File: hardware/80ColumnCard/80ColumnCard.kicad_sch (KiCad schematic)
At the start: 36 parts, among them J1 Apple II Expansion Bus, J2 VIDEO & LIGHT PEN, Q1 2N3904, U1 74LS86, U14 74LS157, U15 74LS157, U16 74LS157, U18 74LS273, U19 MC6845, U2 74LS02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

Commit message: DEV->DEVICE_SELECT
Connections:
- net DEV renamed DEVICE_SELECT
- net ~{DEV} renamed ~{DEVICE_SELECT}
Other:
- moved on the sheet: J1

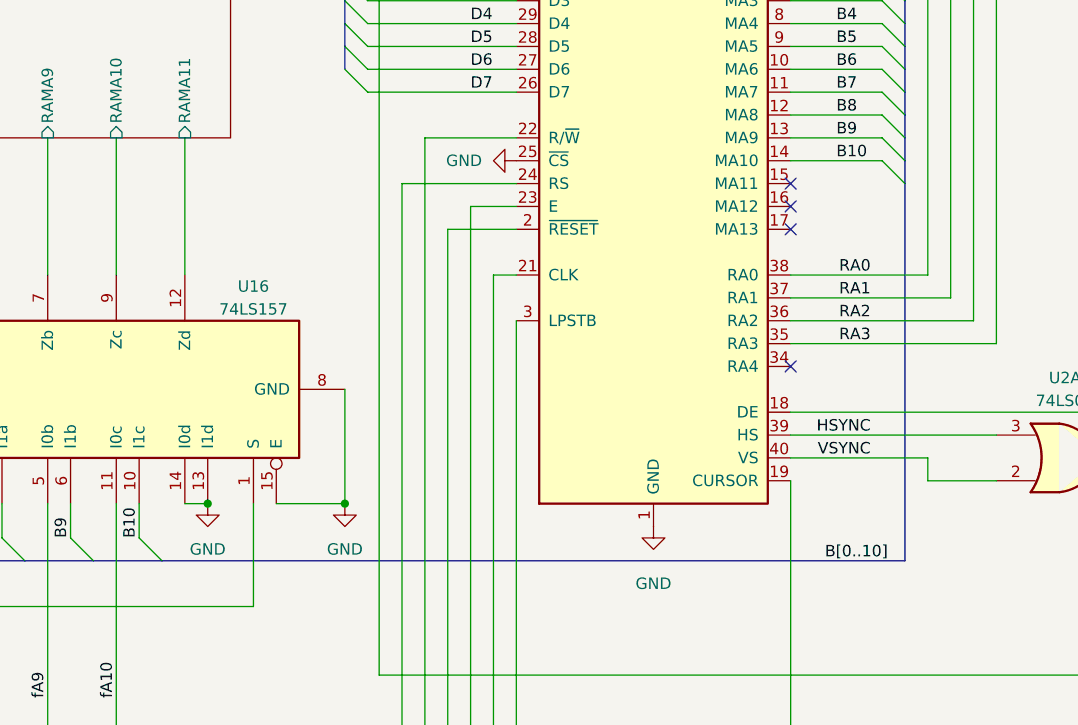
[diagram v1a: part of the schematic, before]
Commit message: connect CRTC A11 to SRAM multiplexer. add jumpers for selectable firmware
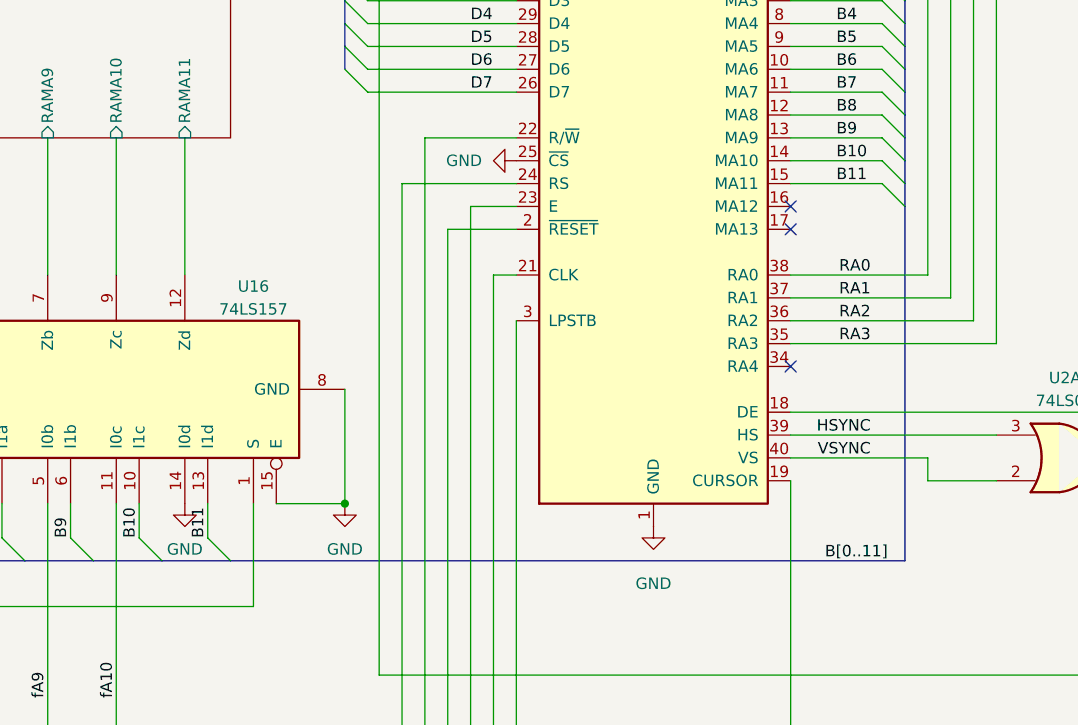
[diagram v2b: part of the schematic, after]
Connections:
- net GND: no longer U16.13 (I1d)
- net B11: now reaches U19.15 (MA11)
- net B11: now also U16.13 (I1d)
- no-connect marks 22 -> 21
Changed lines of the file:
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@@
   (junction (at 60.96 165.1) (diameter 0) (color 0 0 0 0)
   )
-  (junction (at 298.45 167.64) (diameter 0) (color 0 0 0 0)
-  )
   (junction (at 116.84 264.16) (diameter 0) (color 0 0 0 0)
   )
@@
   (no_connect (at 412.75 227.33))
   (no_connect (at 452.12 191.77))
-  (no_connect (at 363.22 132.08))
   (no_connect (at 170.18 40.64))
   (no_connect (at 452.12 186.69))
@@
     (stroke (width 0) (type default) (color 0 0 0 0))
   )
+  (bus_entry (at 298.45 171.45) (size 2.54 2.54)
+    (stroke (width 0) (type default) (color 0 0 0 0))
+  )
   (bus_entry (at 316.23 121.92) (size -2.54 -2.54)
     (stroke (width 0) (type default) (color 0 0 0 0))
@@
     (stroke (width 0) (type default) (color 0 0 0 0))
   )
+  (bus_entry (at 373.38 132.08) (size 2.54 2.54)
+    (stroke (width 0) (type default) (color 0 0 0 0))
+  )
   (bus_entry (at 373.38 129.54) (size 2.54 2.54)
     (stroke (width 0) (type default) (color 0 0 0 0))
@@
     (stroke (width 0) (type default) (color 0 0 0 0))
   )
+  (wire (pts (xy 298.45 167.64) (xy 298.45 171.45))
+    (stroke (width 0) (type default) (color 0 0 0 0))
+  )
   (wire (pts (xy 100.33 261.62) (xy 137.16 261.62))
     (stroke (width 0) (type default) (color 0 0 0 0))
@@
     (stroke (width 0) (type default) (color 0 0 0 0))
   )
+  (bus (pts (xy 300.99 173.99) (xy 375.92 173.99))
+    (stroke (width 0) (type default) (color 0 0 0 0))
+  )
   (wire (pts (xy 275.59 167.64) (xy 275.59 171.45))
     (stroke (width 0) (type default) (color 0 0 0 0))
@@
     (stroke (width 0) (type default) (color 0 0 0 0))
   )
+  (bus (pts (xy 375.92 134.62) (xy 375.92 173.99))
+    (stroke (width 0) (type default) (color 0 0 0 0))
+  )
   (wire (pts (xy 127 58.42) (xy 196.85 58.42))
     (stroke (width 0) (type default) (color 0 0 0 0))
@@
     (stroke (width 0) (type default) (color 0 0 0 0))
   )
-  (bus (pts (xy 293.37 173.99) (xy 375.92 173.99))
+  (bus (pts (xy 293.37 173.99) (xy 300.99 173.99))
     (stroke (width 0) (type default) (color 0 0 0 0))
   )
@@
     (stroke (width 0) (type default) (color 0 0 0 0))
   )
-  (bus (pts (xy 375.92 132.08) (xy 375.92 173.99))
+  (bus (pts (xy 375.92 132.08) (xy 375.92 134.62))
     (stroke (width 0) (type default) (color 0 0 0 0))
   )
@@
     (stroke (width 0) (type default) (color 0 0 0 0))
   )
-  (wire (pts (xy 295.91 167.64) (xy 298.45 167.64))
-    (stroke (width 0) (type default) (color 0 0 0 0))
-  )
   (wire (pts (xy 95.25 204.47) (xy 67.31 204.47))
     (stroke (width 0) (type default) (color 0 0 0 0))
@@
     (stroke (width 0) (type default) (color 0 0 0 0))
   )
+  (wire (pts (xy 363.22 132.08) (xy 373.38 132.08))
+    (stroke (width 0) (type default) (color 0 0 0 0))
+  )
   (wire (pts (xy 224.79 167.64) (xy 224.79 171.45))
     (stroke (width 0) (type default) (color 0 0 0 0))
@@
     (effects (font (size 1.27 1.27)) (justify left bottom))
   )
+  (label "B11" (at 298.45 171.45 90)
+    (effects (font (size 1.27 1.27)) (justify left bottom))
+  )
   (label "A14" (at 535.94 60.96 0)
     (effects (font (size 1.27 1.27)) (justify left bottom))
@@
     (effects (font (size 1.27 1.27)) (justify left bottom))
   )
-  (label "B[0..10]" (at 367.03 173.99 0)
+  (label "B[0..11]" (at 367.03 173.99 0)
     (effects (font (size 1.27 1.27)) (justify left bottom))
   )
@@
     (effects (font (size 1.27 1.27)) (justify left bottom))
   )
+  (label "B11" (at 368.3 132.08 0)
+    (effects (font (size 1.27 1.27)) (justify left bottom))
+  )
   (label "DMA_IN" (at 579.12 81.28 180)
     (effects (font (size 1.27 1.27)) (justify right bottom))
@@
     (pin "1")
   )
-  (symbol (lib_id "power:GND") (at 298.45 167.64 0) (unit 1)
+  (symbol (lib_id "power:GND") (at 295.91 167.64 0) (unit 1)
     (in_bom yes) (on_board yes) (fields_autoplaced)
-    (property "Reference" "#PWR0140" (id 0) (at 298.45 173.99 0)
+    (property "Reference" "#PWR0140" (id 0) (at 295.91 173.99 0)
       (effects (font (size 1.27 1.27)) hide)
     )
-    (property "Value" "GND" (id 1) (at 298.45 172.72 0))
-    (property "Footprint" "" (id 2) (at 298.45 167.64 0)
+    (property "Value" "GND" (id 1) (at 295.91 172.72 0))
+    (property "Footprint" "" (id 2) (at 295.91 167.64 0)
       (effects (font (size 1.27 1.27)) hide)
     )
-    (property "Datasheet" "" (id 3) (at 298.45 167.64 0)
+    (property "Datasheet" "" (id 3) (at 295.91 167.64 0)
       (effects (font (size 1.27 1.27)) hide)
     )
@@
       (reference "#PWR0108") (unit 1) (value "GND") (footprint "")
     )
+    (path "/3653aa16-49ad-4f73-9584-b2d8a31551f4/02f37925-db2f-4b32-9416-ee76e88990e0"
+      (reference "#PWR0109") (unit 1) (value "+5V") (footprint "")
+    )
     (path "/3653aa16-49ad-4f73-9584-b2d8a31551f4/f3066ec5-9040-45a1-98d8-a8bfe2d10528"
       (reference "#PWR0110") (unit 1) (value "GND") (footprint "")
@@
       (reference "J2") (unit 1) (value "VIDEO & LIGHT PEN") (footprint "Connector_PinHeader_2.54mm:PinHeader_1x06_P2.54mm_Horizontal")
     )
+    (path "/3653aa16-49ad-4f73-9584-b2d8a31551f4/9f10952b-85b8-4d29-82d9-c4db269f5aa8"
+      (reference "JP1") (unit 1) (value "A10") (footprint "Connector_PinHeader_2.54mm:PinHeader_1x03_P2.54mm_Vertical")
+    )
+    (path "/3653aa16-49ad-4f73-9584-b2d8a31551f4/ceecdba2-9510-4d35-8da5-2f03008ae102"
+      (reference "JP2") (unit 1) (value "A11") (footprint "Connector_PinHeader_2.54mm:PinHeader_1x03_P2.54mm_Vertical")
+    )
     (path "/5c0e70ea-1119-414b-9aa5-6f54e9ab44e4"

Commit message: clean up, add jumpers for fw/char selection
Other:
- moved on the sheet: C3, C5, J2, Q1, R1, R10, R11, R12, R13, R2, R9, U1A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

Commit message: add some annotations
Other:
- note added: "Char width select"
- note added: "Combined sync"
- note added: "Display enable"
- note added: "Invert signal"
- note added: "Pixel data"
- note added: "SRAM page select"
- note added: "Start at 4 or 5 and count up to 12 to draw either 8 or 9 pixels"
- note added: "video signal"
- moved on the sheet: U4F, U6D
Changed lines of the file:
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@@
   (junction (at 220.98 251.46) (diameter 0) (color 0 0 0 0)
   )
-  (junction (at 160.02 179.07) (diameter 0) (color 0 0 0 0)
-  )
   (junction (at 128.27 189.23) (diameter 0) (color 0 0 0 0)
   )
@@
   (junction (at 41.91 76.2) (diameter 0) (color 0 0 0 0)
   )
+  (junction (at 168.91 179.07) (diameter 0) (color 0 0 0 0)
+  )
   (junction (at 209.55 71.12) (diameter 0) (color 0 0 0 0)
   )
@@
     (stroke (width 0) (type default) (color 0 0 0 0))
   )
-  (wire (pts (xy 128.27 189.23) (xy 154.94 189.23))
+  (wire (pts (xy 128.27 189.23) (xy 149.86 189.23))
     (stroke (width 0) (type default) (color 0 0 0 0))
   )
@@
     (stroke (width 0) (type default) (color 0 0 0 0))
   )
+  (wire (pts (xy 168.91 179.07) (xy 201.93 179.07))
+    (stroke (width 0) (type default) (color 0 0 0 0))
+  )
   (wire (pts (xy 415.29 181.61) (xy 415.29 157.48))
     (stroke (width 0) (type default) (color 0 0 0 0))
@@
     (stroke (width 0) (type default) (color 0 0 0 0))
   )
-  (wire (pts (xy 474.98 196.85) (xy 474.98 219.71))
+  (wire (pts (xy 464.82 196.85) (xy 464.82 219.71))
     (stroke (width 0) (type default) (color 0 0 0 0))
   )
@@
     (stroke (width 0) (type default) (color 0 0 0 0))
   )
-  (wire (pts (xy 100.33 153.67) (xy 138.43 153.67))
+  (wire (pts (xy 100.33 153.67) (xy 133.35 153.67))
     (stroke (width 0) (type default) (color 0 0 0 0))
   )
@@
     (stroke (width 0) (type default) (color 0 0 0 0))
   )
-  (wire (pts (xy 154.94 189.23) (xy 154.94 163.83))
+  (wire (pts (xy 149.86 172.72) (xy 149.86 189.23))
     (stroke (width 0) (type default) (color 0 0 0 0))
   )
@@
     (stroke (width 0) (type default) (color 0 0 0 0))
   )
-  (wire (pts (xy 426.72 219.71) (xy 474.98 219.71))
+  (wire (pts (xy 426.72 219.71) (xy 464.82 219.71))
     (stroke (width 0) (type default) (color 0 0 0 0))
   )
@@
     (stroke (width 0) (type default) (color 0 0 0 0))
   )
-  (wire (pts (xy 97.79 237.49) (xy 97.79 207.01))
+  (wire (pts (xy 97.79 237.49) (xy 97.79 217.17))
     (stroke (width 0) (type default) (color 0 0 0 0))
   )
@@
     (stroke (width 0) (type default) (color 0 0 0 0))
   )
-  (wire (pts (xy 153.67 153.67) (xy 162.56 153.67))
+  (wire (pts (xy 148.59 153.67) (xy 149.86 153.67))
     (stroke (width 0) (type default) (color 0 0 0 0))
   )
@@
     (stroke (width 0) (type default) (color 0 0 0 0))
   )
+  (wire (pts (xy 168.91 170.18) (xy 167.64 170.18))
+    (stroke (width 0) (type default) (color 0 0 0 0))
+  )
   (wire (pts (xy 158.75 255.27) (xy 173.99 255.27))
     (stroke (width 0) (type default) (color 0 0 0 0))
@@
     (stroke (width 0) (type default) (color 0 0 0 0))
   )
+  (wire (pts (xy 130.81 179.07) (xy 168.91 179.07))
+    (stroke (width 0) (type default) (color 0 0 0 0))
+  )
   (wire (pts (xy 196.85 58.42) (xy 196.85 88.9))
     (stroke (width 0) (type default) (color 0 0 0 0))
@@
     (stroke (width 0) (type default) (color 0 0 0 0))
   )
-  (wire (pts (xy 154.94 163.83) (xy 157.48 163.83))
-    (stroke (width 0) (type default) (color 0 0 0 0))
-  )
   (wire (pts (xy 212.09 73.66) (xy 325.12 73.66))
     (stroke (width 0) (type default) (color 0 0 0 0))
@@
     (stroke (width 0) (type default) (color 0 0 0 0))
   )
-  (wire (pts (xy 276.86 207.01) (xy 276.86 241.3))
+  (wire (pts (xy 276.86 217.17) (xy 276.86 241.3))
     (stroke (width 0) (type default) (color 0 0 0 0))
   )
@@
     (stroke (width 0) (type default) (color 0 0 0 0))
   )
+  (wire (pts (xy 149.86 172.72) (xy 152.4 172.72))
+    (stroke (width 0) (type default) (color 0 0 0 0))
+  )
   (wire (pts (xy 434.34 170.18) (xy 434.34 186.69))
     (stroke (width 0) (type default) (color 0 0 0 0))
@@
     (stroke (width 0) (type default) (color 0 0 0 0))
   )
+  (wire (pts (xy 149.86 167.64) (xy 152.4 167.64))
+    (stroke (width 0) (type default) (color 0 0 0 0))
+  )
   (wire (pts (xy 177.8 201.93) (xy 327.66 201.93))
     (stroke (width 0) (type default) (color 0 0 0 0))
@@
     (stroke (width 0) (type default) (color 0 0 0 0))
   )
+  (wire (pts (xy 168.91 170.18) (xy 168.91 179.07))
+    (stroke (width 0) (type default) (color 0 0 0 0))
+  )
   (wire (pts (xy 535.94 33.02) (xy 551.18 33.02))
     (stroke (width 0) (type default) (color 0 0 0 0))
@@
     (stroke (width 0) (type default) (color 0 0 0 0))
   )
-  (wire (pts (xy 97.79 207.01) (xy 276.86 207.01))
+  (wire (pts (xy 97.79 217.17) (xy 276.86 217.17))
     (stroke (width 0) (type default) (color 0 0 0 0))
   )
@@
     (stroke (width 0) (type default) (color 0 0 0 0))
   )
-  (wire (pts (xy 162.56 153.67) (xy 162.56 163.83))
+  (wire (pts (xy 149.86 153.67) (xy 149.86 167.64))
     (stroke (width 0) (type default) (color 0 0 0 0))
   )
-  (wire (pts (xy 462.28 196.85) (xy 474.98 196.85))
+  (wire (pts (xy 462.28 196.85) (xy 464.82 196.85))
     (stroke (width 0) (type default) (color 0 0 0 0))
   )
@@
     (stroke (width 0) (type default) (color 0 0 0 0))
   )
-  (wire (pts (xy 160.02 179.07) (xy 201.93 179.07))
-    (stroke (width 0) (type default) (color 0 0 0 0))
-  )
   (wire (pts (xy 199.39 60.96) (xy 325.12 60.96))
     (stroke (width 0) (type default) (color 0 0 0 0))
@@
     (stroke (width 0) (type default) (color 0 0 0 0))
   )
-  (wire (pts (xy 130.81 179.07) (xy 160.02 179.07))
-    (stroke (width 0) (type default) (color 0 0 0 0))
-  )
   (wire (pts (xy 412.75 201.93) (xy 412.75 228.6))
     (stroke (width 0) (type default) (color 0 0 0 0))
@@
     (stroke (width 0) (type default) (color 0 0 0 0))
   )
+  (text "video signal" (at 520.7 123.19 0)
+    (effects (font (size 1.27 1.27)) (justify left bottom))
+  )
+  (text "Display enable" (at 480.06 120.65 0)
+    (effects (font (size 1.27 1.27)) (justify left bottom))
+  )
+  (text "Combined sync" (at 515.62 148.59 0)
+    (effects (font (size 1.27 1.27)) (justify left bottom))
+  )
+  (text "SRAM page select" (at 138.43 233.68 0)
+    (effects (font (size 1.27 1.27)) (justify left bottom))
+  )
+  (text "Pixel data" (at 459.74 109.22 0)
+    (effects (font (size 1.27 1.27)) (justify left bottom))
+  )
   (text "Apple II Peripheral Connector" (at 539.75 15.24 0)
     (effects (font (size 1.524 1.524)) (justify left bottom))
   )
+  (text "Start at 4 or 5\nand count up to 12\nto draw either 8 or 9 pixels"
+    (at 276.86 223.52 0)
+    (effects (font (size 1.27 1.27)) (justify left bottom))
+  )
+  (text "Char width select" (at 97.79 233.68 0)
+    (effects (font (size 1.27 1.27)) (justify left bottom))
+  )
+  (text "Invert signal" (at 457.2 116.84 0)
+    (effects (font (size 1.27 1.27)) (justify left bottom))
+  )
   (label "E6" (at 325.12 71.12 180)
     (effects (font (size 1.27 1.27)) (justify right bottom))
@@
     (effects (font (size 1.27 1.27)) (justify left bottom))
   )
-  (label "RAM_~{A}{slash}B" (at 161.29 179.07 0)
+  (label "RAM_~{A}{slash}B" (at 160.02 179.07 0)
     (effects (font (size 1.27 1.27)) (justify left bottom))
   )
@@
     (pin "1")
   )
-  (symbol (lib_id "74xx:74LS00") (at 160.02 171.45 90) (mirror x) (unit 4)
+  (symbol (lib_id "74xx:74LS00") (at 160.02 170.18 0) (mirror x) (unit 4)
     (in_bom yes) (on_board yes) (fields_autoplaced)
-    (property "Reference" "U6" (id 0) (at 165.1 170.1799 90)
+    (property "Reference" "U6" (id 0) (at 158.7499 165.1 90)
       (effects (font (size 1.27 1.27)) (justify right))
     )
-    (property "Value" "74LS00" (id 1) (at 165.1 172.7199 90)
+    (property "Value" "74LS00" (id 1) (at 161.2899 165.1 90)
       (effects (font (size 1.27 1.27)) (justify right))
     )
-    (property "Footprint" "MyPackages:DIP-14_W7.62mm" (id 2) (at 160.02 171.45 0)
+    (property "Footprint" "MyPackages:DIP-14_W7.62mm" (id 2) (at 160.02 170.18 0)
       (effects (font (size 1.27 1.27)) hide)
     )
-    (property "Datasheet" "http://www.ti.com/lit/gpn/sn74ls00" (id 3) (at 160.02 171.45 0)
+    (property "Datasheet" "http://www.ti.com/lit/gpn/sn74ls00" (id 3) (at 160.02 170.18 0)
       (effects (font (size 1.27 1.27)) hide)
     )
@@
     (pin "1")
   )
-  (symbol (lib_id "74xx:74LS04") (at 146.05 153.67 0) (unit 6)
+  (symbol (lib_id "74xx:74LS04") (at 140.97 153.67 0) (unit 6)
     (in_bom yes) (on_board yes) (fields_autoplaced)
-    (property "Reference" "U4" (id 0) (at 146.05 144.78 0))
-    (property "Value" "74LS04" (id 1) (at 146.05 147.32 0))
-    (property "Footprint" "MyPackages:DIP-14_W7.62mm" (id 2) (at 146.05 153.67 0)
+    (property "Reference" "U4" (id 0) (at 140.97 144.78 0))
+    (property "Value" "74LS04" (id 1) (at 140.97 147.32 0))
+    (property "Footprint" "MyPackages:DIP-14_W7.62mm" (id 2) (at 140.97 153.67 0)
       (effects (font (size 1.27 1.27)) hide)
     )
-    (property "Datasheet" "http://www.ti.com/lit/gpn/sn74LS04" (id 3) (at 146.05 153.67 0)
+    (property "Datasheet" "http://www.ti.com/lit/gpn/sn74LS04" (id 3) (at 140.97 153.67 0)
       (effects (font (size 1.27 1.27)) hide)
     )

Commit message: use more common component sizes
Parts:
- C1, C4: footprint MyPassives:CP_Radial_Tantal_D4.5mm_P6.35mm -> Capacitor_THT:CP_Radial_Tantal_D4.5mm_P5.00mm
- C2, C3, C5: footprint MyPassives:C_Axial_L2.6mm_D1.8mm_P6.35mm_Horizontal -> Capacitor_THT:C_Disc_D4.3mm_W1.9mm_P5.00mm
- CR1: footprint Diode_THT:D_DO-35_SOD27_P10.16mm_Horizontal -> Diode_THT:D_DO-35_SOD27_P7.62mm_Horizontal
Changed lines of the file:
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@@
       (effects (font (size 1.27 1.27)) (justify left))
     )
-    (property "Footprint" "MyPassives:C_Axial_L2.6mm_D1.8mm_P6.35mm_Horizontal" (id 2) (at 117.8052 273.05 0)
+    (property "Footprint" "Capacitor_THT:C_Disc_D4.3mm_W1.9mm_P5.00mm" (id 2) (at 117.8052 273.05 0)
       (effects (font (size 1.27 1.27)) hide)
     )
@@
       (effects (font (size 1.27 1.27)) (justify right))
     )
-    (property "Footprint" "MyPassives:CP_Radial_Tantal_D4.5mm_P6.35mm" (id 2) (at 89.2048 299.72 0)
+    (property "Footprint" "Capacitor_THT:CP_Radial_Tantal_D4.5mm_P5.00mm" (id 2) (at 89.2048 299.72 0)
       (effects (font (size 1.27 1.27)) hide)
     )
@@
       (effects (font (size 1.27 1.27)) (justify left))
     )
-    (property "Footprint" "MyPassives:CP_Radial_Tantal_D4.5mm_P6.35mm" (id 2) (at 45.4152 45.72 0)
+    (property "Footprint" "Capacitor_THT:CP_Radial_Tantal_D4.5mm_P5.00mm" (id 2) (at 45.4152 45.72 0)
       (effects (font (size 1.27 1.27)) hide)
     )
@@
     (property "Reference" "C3" (id 0) (at 214.63 243.84 90))
     (property "Value" "1nF" (id 1) (at 214.63 246.38 90))
-    (property "Footprint" "MyPassives:C_Axial_L2.6mm_D1.8mm_P6.35mm_Horizontal" (id 2) (at 218.44 250.4948 0)
+    (property "Footprint" "Capacitor_THT:C_Disc_D4.3mm_W1.9mm_P5.00mm" (id 2) (at 218.44 250.4948 0)
       (effects (font (size 1.27 1.27)) hide)
     )
@@
       (effects (font (size 1.27 1.27)) (justify right))
     )
-    (property "Footprint" "Diode_THT:D_DO-35_SOD27_P10.16mm_Horizontal" (id 2) (at 112.395 182.88 0)
+    (property "Footprint" "Diode_THT:D_DO-35_SOD27_P7.62mm_Horizontal" (id 2) (at 112.395 182.88 0)
       (effects (font (size 1.27 1.27)) hide)
     )
@@
       (effects (font (size 1.27 1.27)) (justify left))
     )
-    (property "Footprint" "MyPassives:C_Axial_L2.6mm_D1.8mm_P6.35mm_Horizontal" (id 2) (at 550.8752 127 0)
+    (property "Footprint" "Capacitor_THT:C_Disc_D4.3mm_W1.9mm_P5.00mm" (id 2) (at 550.8752 127 0)
       (effects (font (size 1.27 1.27)) hide)
     )
@@
     )
     (path "/1c471e17-2062-4fa9-afba-c8585dc0f28e"
-      (reference "C1") (unit 1) (value ".1uF") (footprint "MyPassives:CP_Radial_Tantal_D4.5mm_P6.35mm")
+      (reference "C1") (unit 1) (value ".1uF") (footprint "Capacitor_THT:CP_Radial_Tantal_D4.5mm_P5.00mm")
     )
     (path "/0e23a83b-30d9-4a6e-9a2e-d6060d697b61"
-      (reference "C2") (unit 1) (value ".1nF") (footprint "MyPassives:C_Axial_L2.6mm_D1.8mm_P6.35mm_Horizontal")
+      (reference "C2") (unit 1) (value ".1nF") (footprint "Capacitor_THT:C_Disc_D4.3mm_W1.9mm_P5.00mm")
     )
     (path "/6fc7b5e8-ff4f-4ca1-8311-c4a7371db1e0"
-      (reference "C3") (unit 1) (value "1nF") (footprint "MyPassives:C_Axial_L2.6mm_D1.8mm_P6.35mm_Horizontal")
+      (reference "C3") (unit 1) (value "1nF") (footprint "Capacitor_THT:C_Disc_D4.3mm_W1.9mm_P5.00mm")
     )
     (path "/542afdf8-b18a-4b8b-b41d-11f54f1d697b"
-      (reference "C4") (unit 1) (value "not placed") (footprint "MyPassives:CP_Radial_Tantal_D4.5mm_P6.35mm")
+      (reference "C4") (unit 1) (value "not placed") (footprint "Capacitor_THT:CP_Radial_Tantal_D4.5mm_P5.00mm")
     )
     (path "/b16d08e5-b57c-421e-8f54-671039c499cf"
-      (reference "C5") (unit 1) (value ".1uF") (footprint "MyPassives:C_Axial_L2.6mm_D1.8mm_P6.35mm_Horizontal")
+      (reference "C5") (unit 1) (value ".1uF") (footprint "Capacitor_THT:C_Disc_D4.3mm_W1.9mm_P5.00mm")
     )
     (path "/a51de418-b2dc-4223-a462-9131f69fc484"
-      (reference "CR1") (unit 1) (value "1N4148") (footprint "Diode_THT:D_DO-35_SOD27_P10.16mm_Horizontal")
+      (reference "CR1") (unit 1) (value "1N4148") (footprint "Diode_THT:D_DO-35_SOD27_P7.62mm_Horizontal")
     )
     (path "/2dc540c8-1e8a-4740-8811-dc4413a0ee4b"
